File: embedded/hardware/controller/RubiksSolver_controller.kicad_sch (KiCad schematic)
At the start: 16 parts

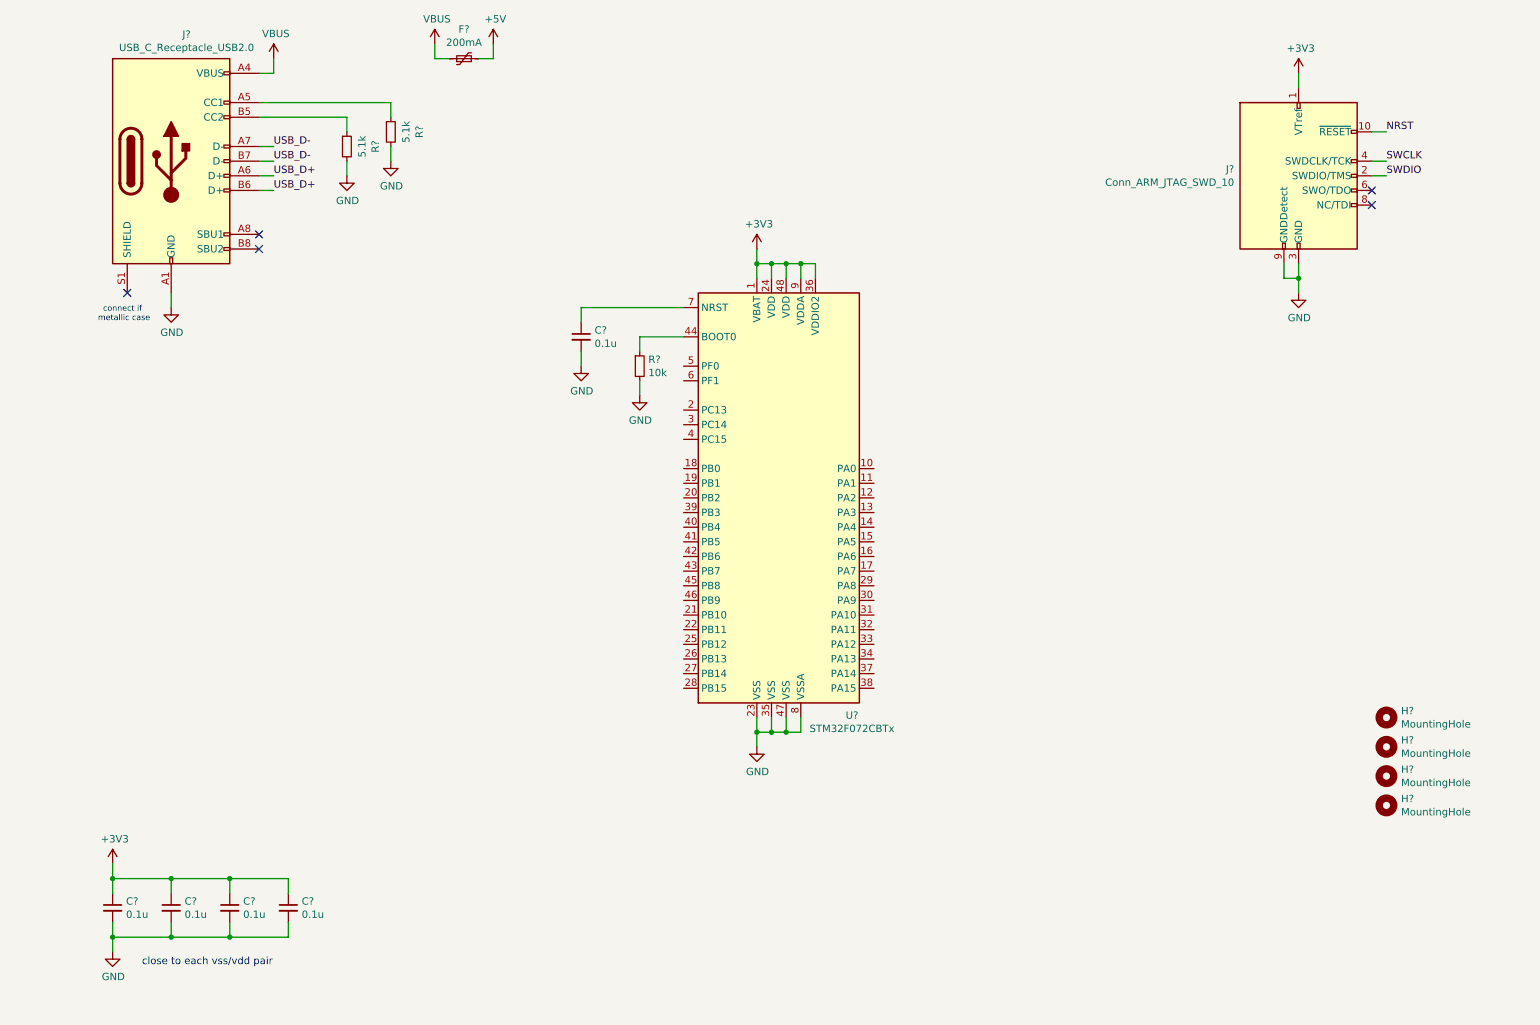
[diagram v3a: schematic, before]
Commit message: Add 3v3 regulator, 24v input, power mux, motors without drivers
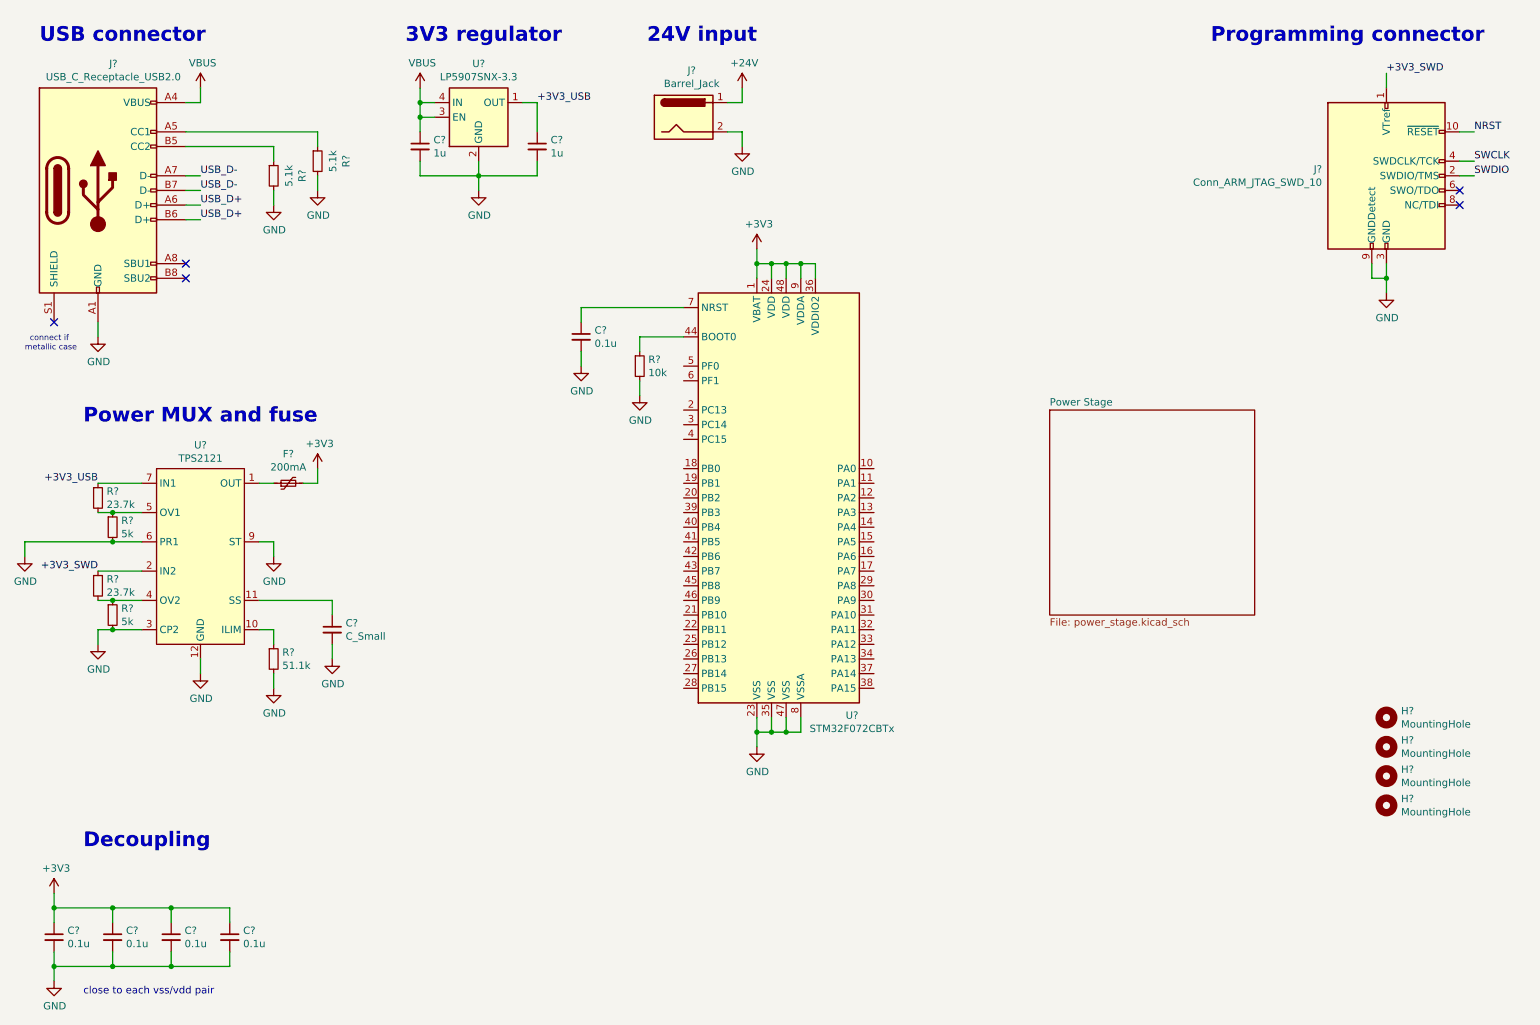
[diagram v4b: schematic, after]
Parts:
- added C? (x2): 1u, symbol Device:C_Small
- added C?: C_Small, symbol Device:C_Small
- added J?: Barrel_Jack, symbol Connector:Barrel_Jack
- added R? (x2): 23.7k, symbol Device:R_Small
- added R?: 51.1k, symbol Device:R_Small
- added R? (x2): 5k, symbol Device:R_Small
- added U?: TPS2121, symbol User:TPS2121
- added U?: LP5907SNX-3.3, User:Texas_X2SON-4_1x1mm_P0.65mm, symbol User:LP5907SNX-3.3
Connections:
- net +5V is gone; now on net +3V3: F?.2
- net +3V3: no longer J?.1 (VTref)
- net GND: now also C?.2, C?.2, C?.2, J?.2, R?.2, R?.2, R?.2, U?.12 (GND), U?.2 (GND), U?.3 (CP2), U?.5 (GND), U?.6 (PR1), U?.9 (ST)
- net VBUS: now also C?.1, U?.3 (EN), U?.4 (IN); no longer F?.1
- new net: R?.1, R?.2, U?.4 (OV2)
- new net: F?.1, U?.1 (OUT), U?.8 (OUT)
- new net: R?.1, U?.10 (ILIM)
- new net: C?.1, U?.11 (SS)
- new net: R?.1, R?.2, U?.5 (OV1)
- new net +24V: J?.1
- new net +3V3_SWD: J?.1 (VTref), R?.1, U?.2 (IN2)
- new net +3V3_USB: C?.1, R?.1, U?.1 (OUT), U?.7 (IN1)
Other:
- added sheet Power Stage (power_stage.kicad_sch)
- note added: "24V input"
- note added: "3V3 regulator"
- note added: "Decoupling"
- note added: "Power MUX and fuse"
- note added: "Programming connector"
- note added: "USB connector"
- moved on the sheet: C?, F?, J?, R?

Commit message: Change for a bigger MCU, add place multiplexer for USART
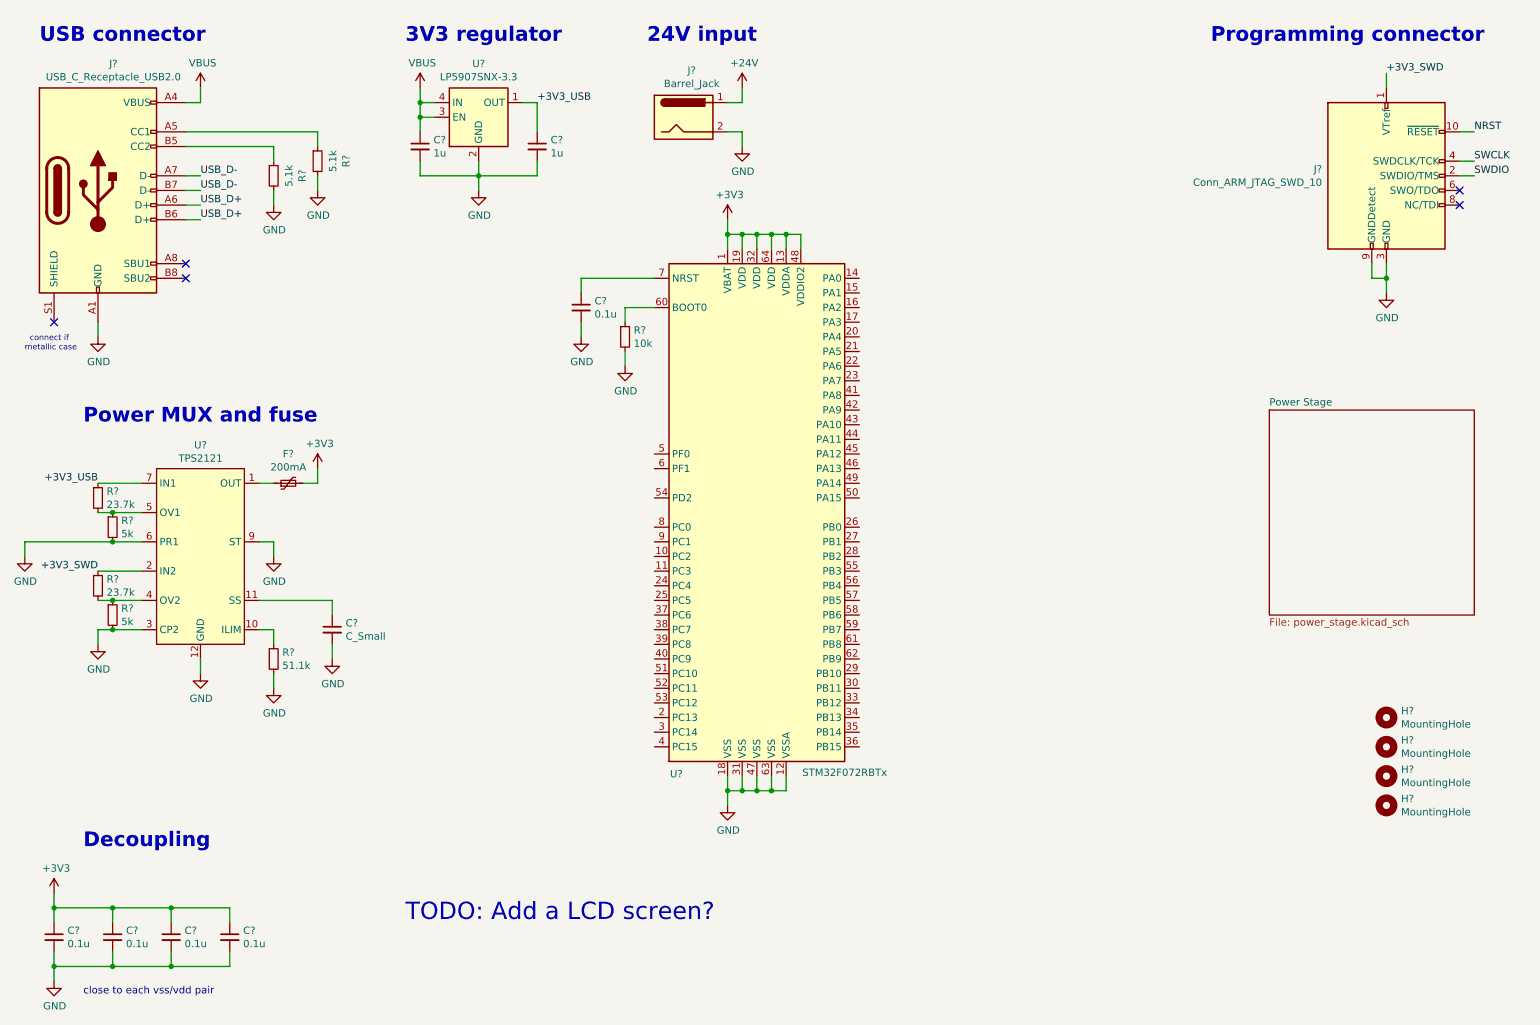
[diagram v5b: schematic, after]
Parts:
- removed U?: STM32F072CBTx, Package_QFP:LQFP-48_7x7mm_P0.5mm, symbol MCU_ST_STM32F0:STM32F072CBTx
- added U?: STM32F072RBTx, Package_QFP:LQFP-64_10x10mm_P0.5mm, symbol MCU_ST_STM32F0:STM32F072RBTx
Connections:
- net +3V3: now also U?.1 (VBAT), U?.13 (VDDA), U?.19 (VDD), U?.32 (VDD), U?.48 (VDDIO2), U?.64 (VDD)
- net GND: now also U?.12 (VSSA), U?.18 (VSS), U?.31 (VSS), U?.47 (VSS), U?.63 (VSS)
- net at R?.1: now also U?.60 (BOOT0)
- net at C?.1: now also U?.7 (NRST)
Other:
- note added: "TODO: Add a LCD screen?"
- moved on the sheet: C?, R?
